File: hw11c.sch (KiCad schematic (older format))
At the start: 61 parts, among them Q1 KX-7_12MHZ, SW1 BUTT1, SW2 BUTT2, X1 ~RESET, X10 PIO2.8, X11 PIO1.4, X12 PAD, X13 PIO0.8, X14 PIO0.9, X2 SWCLK, X3 SWDIO, X4 SSEL1, X5 SCK1, X6 MISO1, X7 MOSI1, X8 PIO2.6, X9 PIO2.7

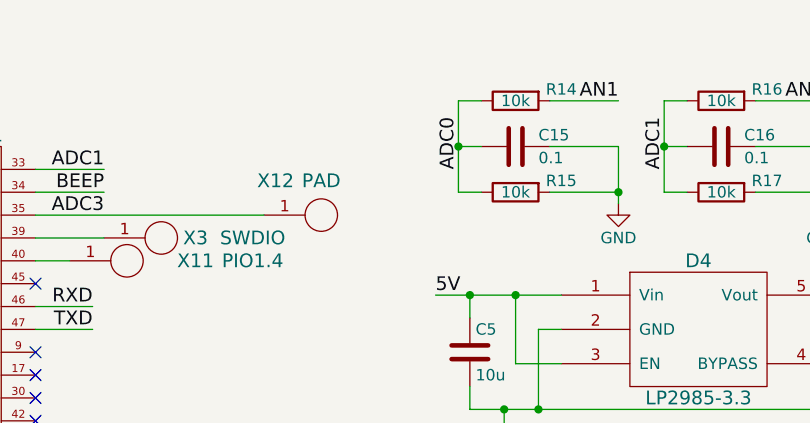
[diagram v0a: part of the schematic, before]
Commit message: Add termistor support in AN1 channel. Fix silk layer in board.
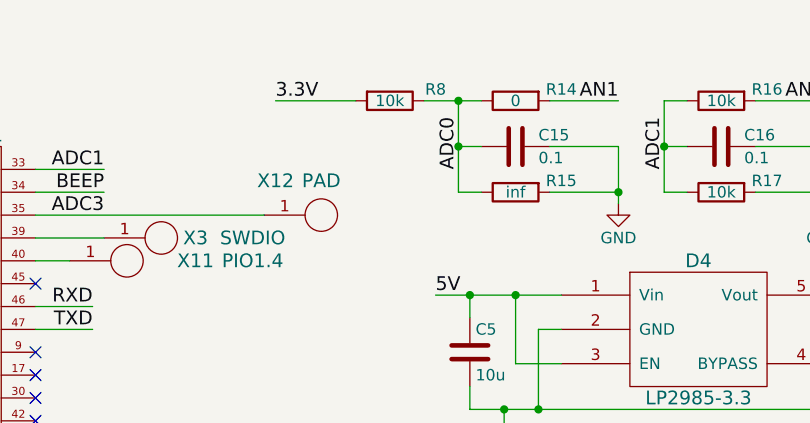
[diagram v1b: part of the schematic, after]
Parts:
- added R8: 10k, libs:R_0603, symbol R
- R14: value 10k -> 0
- R15: value 10k -> inf
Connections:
- net 3.3V: now also R8.2
- net ADC0: now also R8.1
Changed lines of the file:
@@
 $EndComp
 $Comp
-L GND #PWR016
+L GND #PWR015
 U 1 1 57B35E36
 P 8800 2400
-F 0 "#PWR016" H 8800 2150 50  0001 C CNN
+F 0 "#PWR015" H 8800 2150 50  0001 C CNN
 F 1 "GND" H 8800 2250 50  0000 C CNN
 F 2 "" H 8800 2400 50  0000 C CNN
@@
 $EndComp
 $Comp
-L GND #PWR017
+L GND #PWR016
 U 1 1 57B3CAEB
 P 9700 2400
-F 0 "#PWR017" H 9700 2150 50  0001 C CNN
+F 0 "#PWR016" H 9700 2150 50  0001 C CNN
 F 1 "GND" H 9700 2250 50  0000 C CNN
 F 2 "" H 9700 2400 50  0000 C CNN
@@
 P 7450 1950
 F 0 "R14" V 7400 1750 50  0000 C CNN
-F 1 "10k" V 7450 1950 50  0000 C CNN
+F 1 "0" V 7450 1950 50  0000 C CNN
 F 2 "libs:R_0603" V 7380 1950 50  0001 C CNN
 F 3 "" H 7450 1950 50  0000 C CNN
@@
 P 7450 2350
 F 0 "R15" V 7400 2150 50  0000 C CNN
-F 1 "10k" V 7450 2350 50  0000 C CNN
+F 1 "inf" V 7450 2350 50  0000 C CNN
 F 2 "libs:R_0603" V 7380 2350 50  0001 C CNN
 F 3 "" H 7450 2350 50  0000 C CNN
@@
 $EndComp
 $Comp
-L GND #PWR018
+L GND #PWR017
 U 1 1 57B3CC49
 P 7900 2400
-F 0 "#PWR018" H 7900 2150 50  0001 C CNN
+F 0 "#PWR017" H 7900 2150 50  0001 C CNN
 F 1 "GND" H 7900 2250 50  0000 C CNN
 F 2 "" H 7900 2400 50  0000 C CNN
@@
 	7200 2350 7300 2350
 Wire Wire Line
-	7300 1950 7200 1950
+	7050 1950 7300 1950
 Wire Wire Line
 	7200 1950 7200 2350
@@
 Wire Wire Line
 	2350 1700 2800 1700
+$Comp
+L R R8
+U 1 1 5A3BC45E
+P 6900 1950
+F 0 "R8" V 6850 2150 50  0000 C CNN
+F 1 "10k" V 6900 1950 50  0000 C CNN
+F 2 "libs:R_0603" V 6830 1950 50  0001 C CNN
+F 3 "" H 6900 1950 50  0000 C CNN
+	1    6900 1950
+	0    1    1    0
+$EndComp
+Connection ~ 7200 1950
+Text Label 6400 1950 0    60   ~ 0
+3.3V
+Wire Wire Line
+	6400 1950 6750 1950
 $EndSCHEMATC

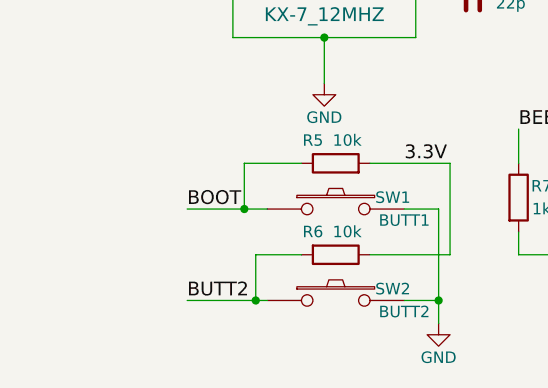
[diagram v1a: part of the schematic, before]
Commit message: Add connector for external buttons.
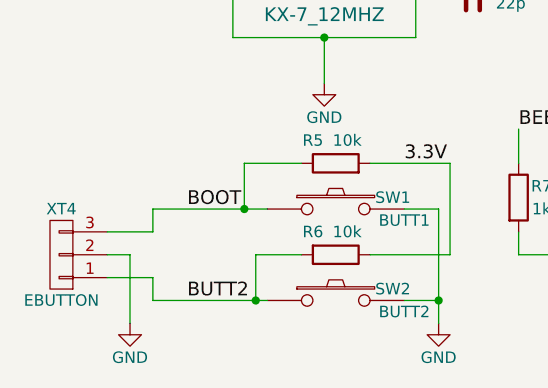
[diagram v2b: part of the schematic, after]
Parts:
- added XT4: EBUTTON, libs:Pin_Header_Straight_1x03, symbol CONN_01X03
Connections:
- net BOOT: now also XT4.3 (P3)
- net BUTT2: now also XT4.1 (P1)
- net GND: now also XT4.2 (P2)
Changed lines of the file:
@@
 	2700 2350 2950 2350
 Wire Wire Line
-	1350 6200 1700 6200
-Wire Wire Line
-	1350 5800 1700 5800
+	1200 6200 1700 6200
+Wire Wire Line
+	1200 5800 1700 5800
 Connection ~ 2450 6200
 Wire Wire Line
@@
 Wire Wire Line
 	6400 1950 6750 1950
+$Comp
+L CONN_01X03 XT4
+U 1 1 5A435FB1
+P 800 6000
+F 0 "XT4" H 800 5800 50  0000 C CNN
+F 1 "EBUTTON" H 800 6200 50  0000 C CNN
+F 2 "libs:Pin_Header_Straight_1x03" H 800 6000 50  0001 C CNN
+F 3 "" H 800 6000 50  0000 C CNN
+	1    800  6000
+	-1   0    0    1
+$EndComp
+$Comp
+L GND #PWR018
+U 1 1 5A4360C5
+P 1100 6300
+F 0 "#PWR018" H 1100 6050 50  0001 C CNN
+F 1 "GND" H 1100 6150 50  0000 C CNN
+F 2 "" H 1100 6300 50  0000 C CNN
+F 3 "" H 1100 6300 50  0000 C CNN
+	1    1100 6300
+	1    0    0    -1
+$EndComp
+Wire Wire Line
+	1100 6300 1100 6000
+Wire Wire Line
+	1100 6000 1000 6000
+Wire Wire Line
+	1000 6100 1200 6100
+Wire Wire Line
+	1200 6100 1200 6200
+Wire Wire Line
+	1200 5800 1200 5900
+Wire Wire Line
+	1200 5900 1000 5900
 $EndSCHEMATC

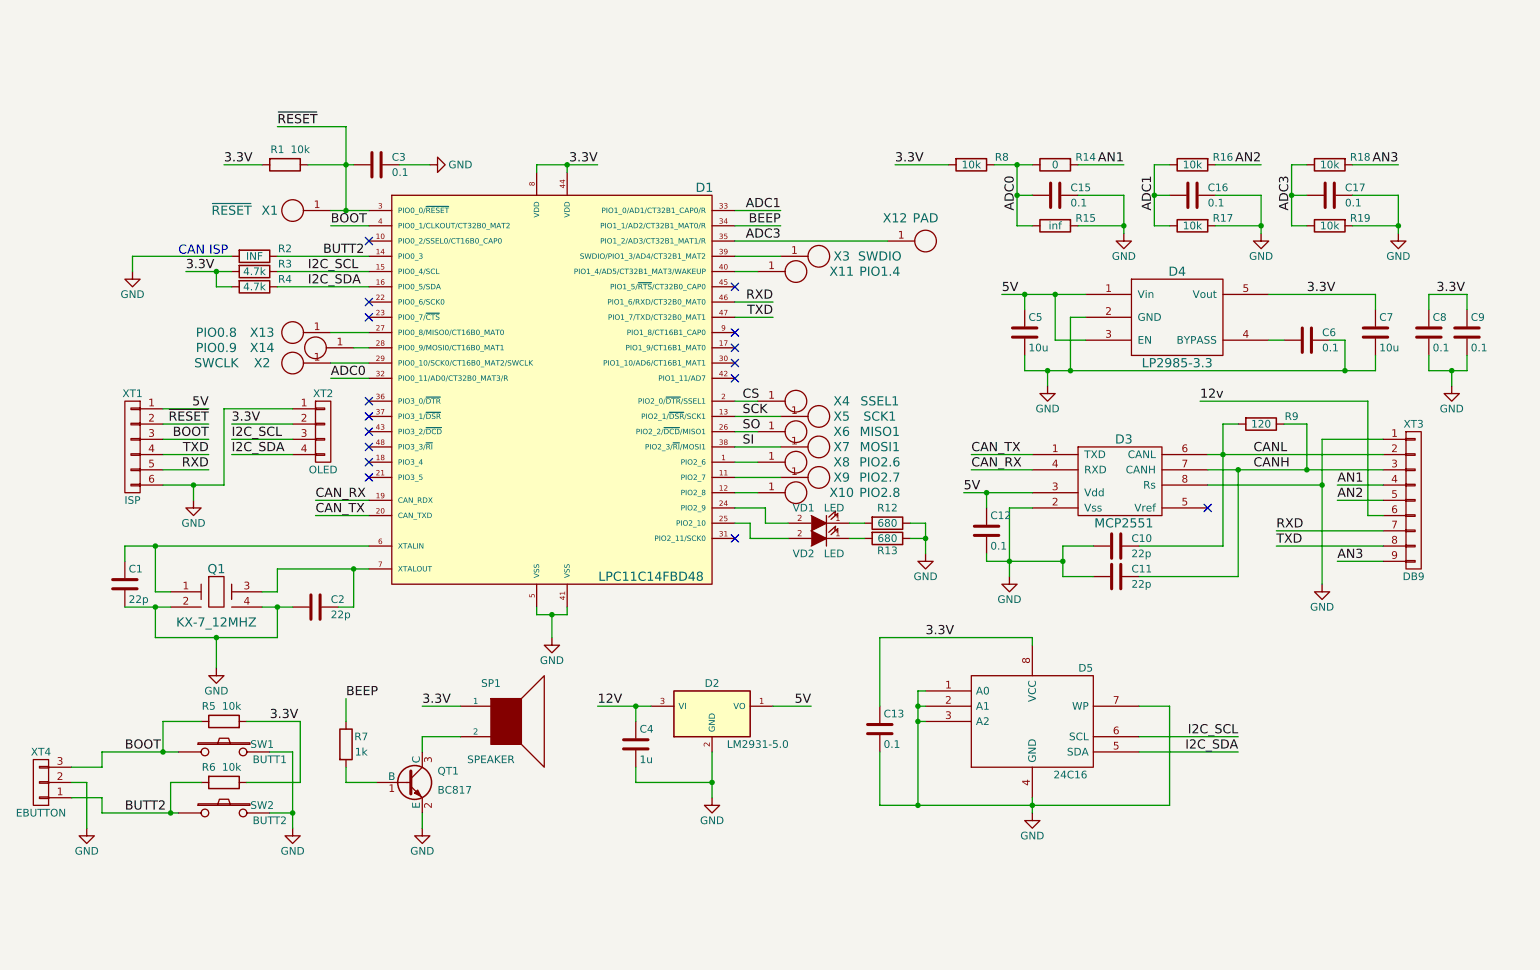
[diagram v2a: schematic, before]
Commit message: Replace XT4 to XT5, more pins in connector (P3.0 and P3.1 to extern).
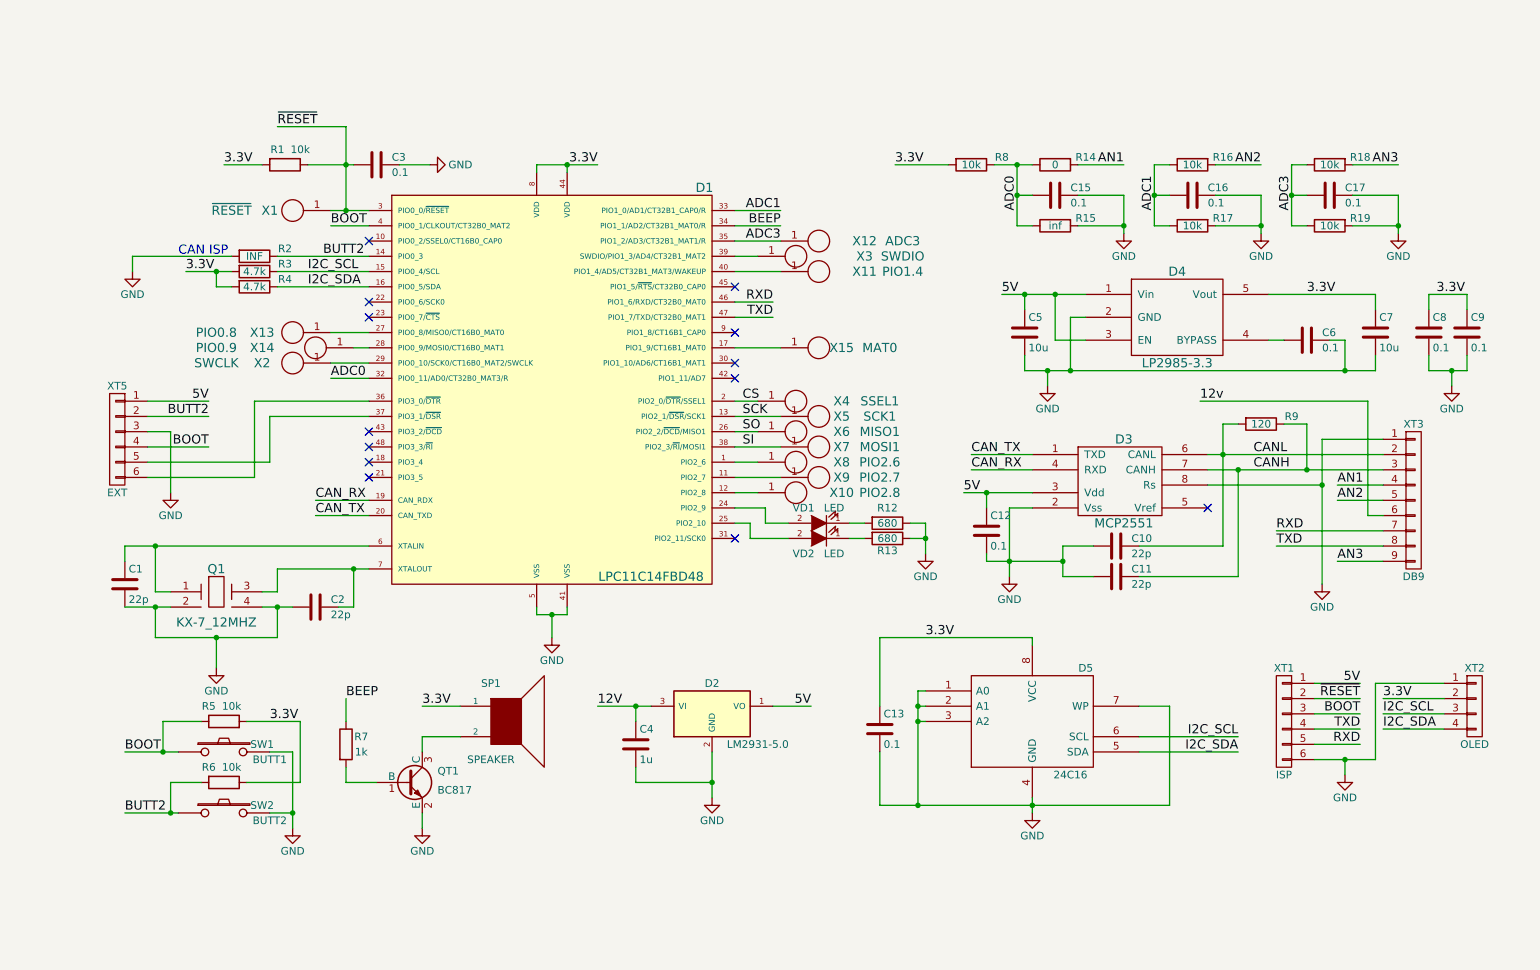
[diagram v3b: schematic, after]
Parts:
- removed XT4: EBUTTON, libs:Pin_Header_Straight_1x03, symbol CONN_01X03
- added X15: MAT0, libs:PAD, symbol PAD
- added XT5: EXT, libs:Pin_Header_Straight_1x06, symbol CONN_01X06
- X12: value PAD -> ADC3
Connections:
- net 5V: now also XT5.1 (P1)
- net BOOT: now also XT5.4 (P4)
- net BUTT2: now also XT5.2 (P2)
- net GND: now also XT5.3 (P3)
- net at D1.17 (PIO1_9/CT16B1_MAT0): now also X15.1
- net at D1.36 (PIO3_0/~DTR~): now also XT5.6 (P6)
- net at D1.37 (PIO3_1/~DSR~): now also XT5.5 (P5)
- no-connect marks 16 -> 13
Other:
- moved on the sheet: X11, X12, X3, XT1, XT2

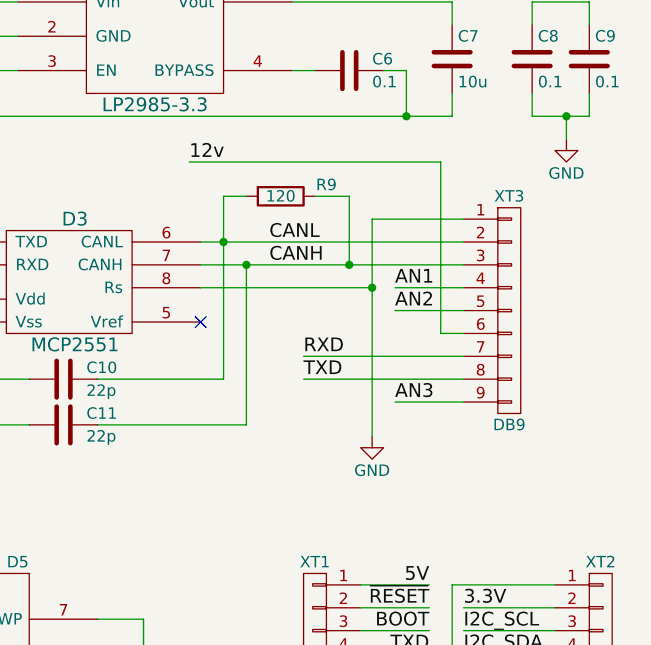
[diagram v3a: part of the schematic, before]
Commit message: Add R10, R11 to RX and TX lines.
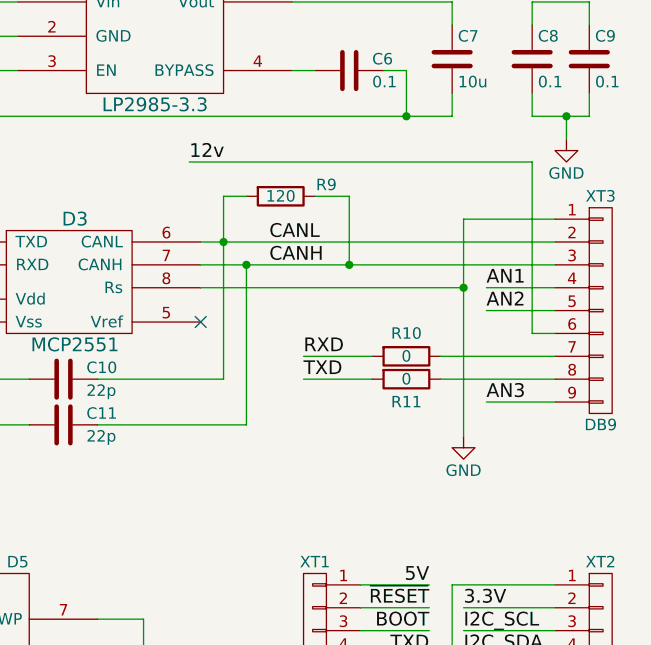
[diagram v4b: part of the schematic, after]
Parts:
- added R10, R11: 0, libs:R_0603, symbol R
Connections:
- net RXD: now also R10.2; no longer XT3.7 (P7)
- net TXD: now also R11.2; no longer XT3.8 (P8)
- new net: R10.1, XT3.7 (P7)
- new net: R11.1, XT3.8 (P8)
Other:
- moved on the sheet: XT3

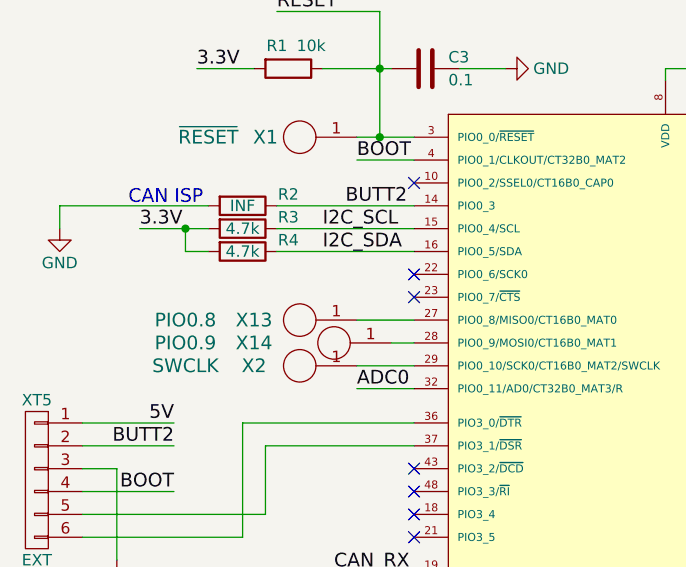
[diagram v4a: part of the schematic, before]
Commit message: Add X16/X17 pads. Fix buttons silk.
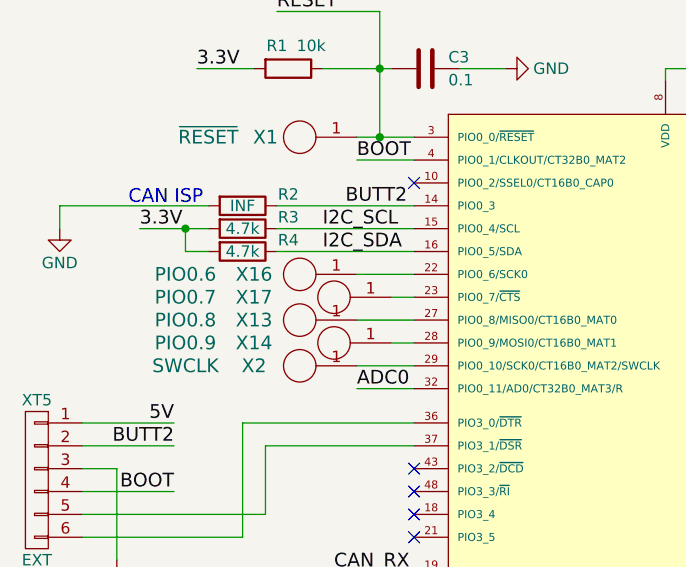
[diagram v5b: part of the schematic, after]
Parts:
- added X16: PIO0.6, libs:PAD, symbol PAD
- added X17: PIO0.7, libs:PAD, symbol PAD
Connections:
- net at D1.22 (PIO0_6/SCK0): now also X16.1
- net at D1.23 (PIO0_7/~CTS~): now also X17.1
- no-connect marks 13 -> 11
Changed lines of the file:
@@
 NoConn ~ 2950 3900
 NoConn ~ 2950 4000
-NoConn ~ 2950 2950
-NoConn ~ 2950 2850
 Text Label 5650 2350 2    60   ~ 0
 BEEP
@@
 Wire Wire Line
 	9200 4450 8900 4450
+$Comp
+L PAD X16
+U 1 1 5A65EB19
+P 2450 2850
+F 0 "X16" H 2250 2850 60  0000 C CNN
+F 1 "PIO0.6" H 1950 2850 60  0000 C CNN
+F 2 "libs:PAD" H 2450 2850 60  0001 C CNN
+F 3 "" H 2450 2850 60  0000 C CNN
+	1    2450 2850
+	1    0    0    -1
+$EndComp
+$Comp
+L PAD X17
+U 1 1 5A65EF6D
+P 2600 2950
+F 0 "X17" H 2250 2950 60  0000 C CNN
+F 1 "PIO0.7" H 1950 2950 60  0000 C CNN
+F 2 "libs:PAD" H 2600 2950 60  0001 C CNN
+F 3 "" H 2600 2950 60  0000 C CNN
+	1    2600 2950
+	1    0    0    -1
+$EndComp
+Wire Wire Line
+	2950 2950 2850 2950
+Wire Wire Line
+	2950 2850 2700 2850
 $EndSCHEMATC
